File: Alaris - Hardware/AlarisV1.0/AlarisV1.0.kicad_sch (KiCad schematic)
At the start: 55 parts, among them J1 MSD-1-A, J2 MTSW-101, J3 636101111001, Q1 BSS138, Q2 BSS138, U1 STM32F401RCTx, U2 BNO055, U3 BMP390L, U4 MS5611-01BA, U5 ICM-20948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

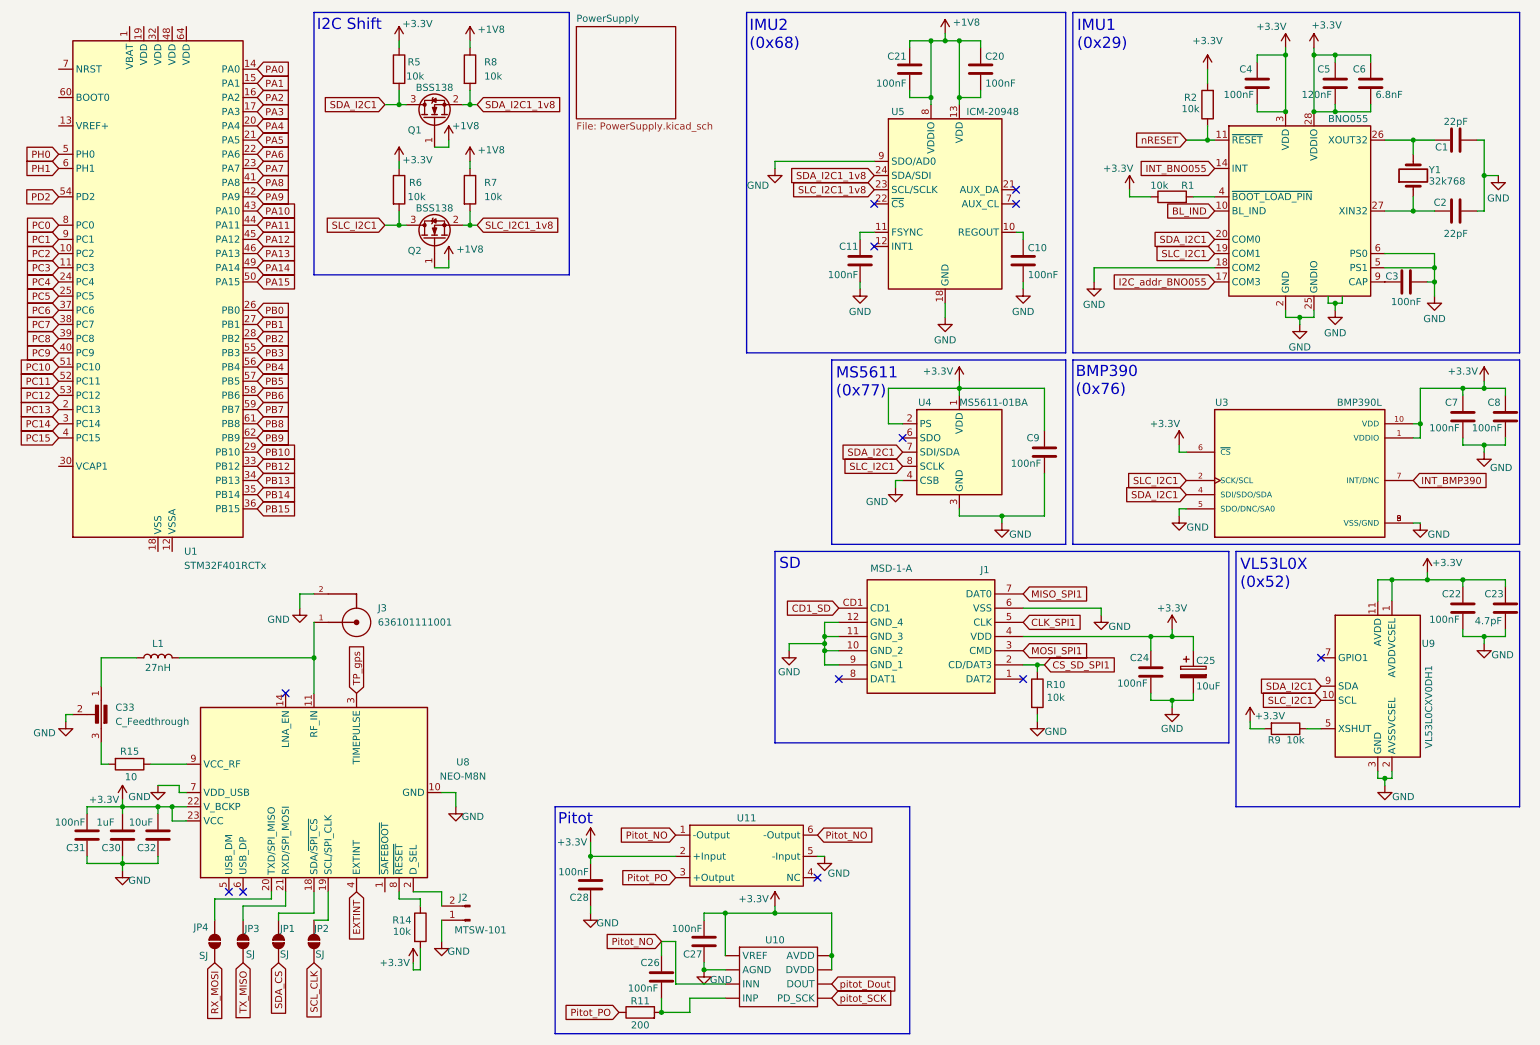
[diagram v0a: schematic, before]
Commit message: Desenvolvimento do Hardware
Desenvolvido os modulos de DAPN, GNCN, LDIN

Ainda é necessario implementação de alguns sensores, e melhor o modulo de gerenciamento de energia da placa
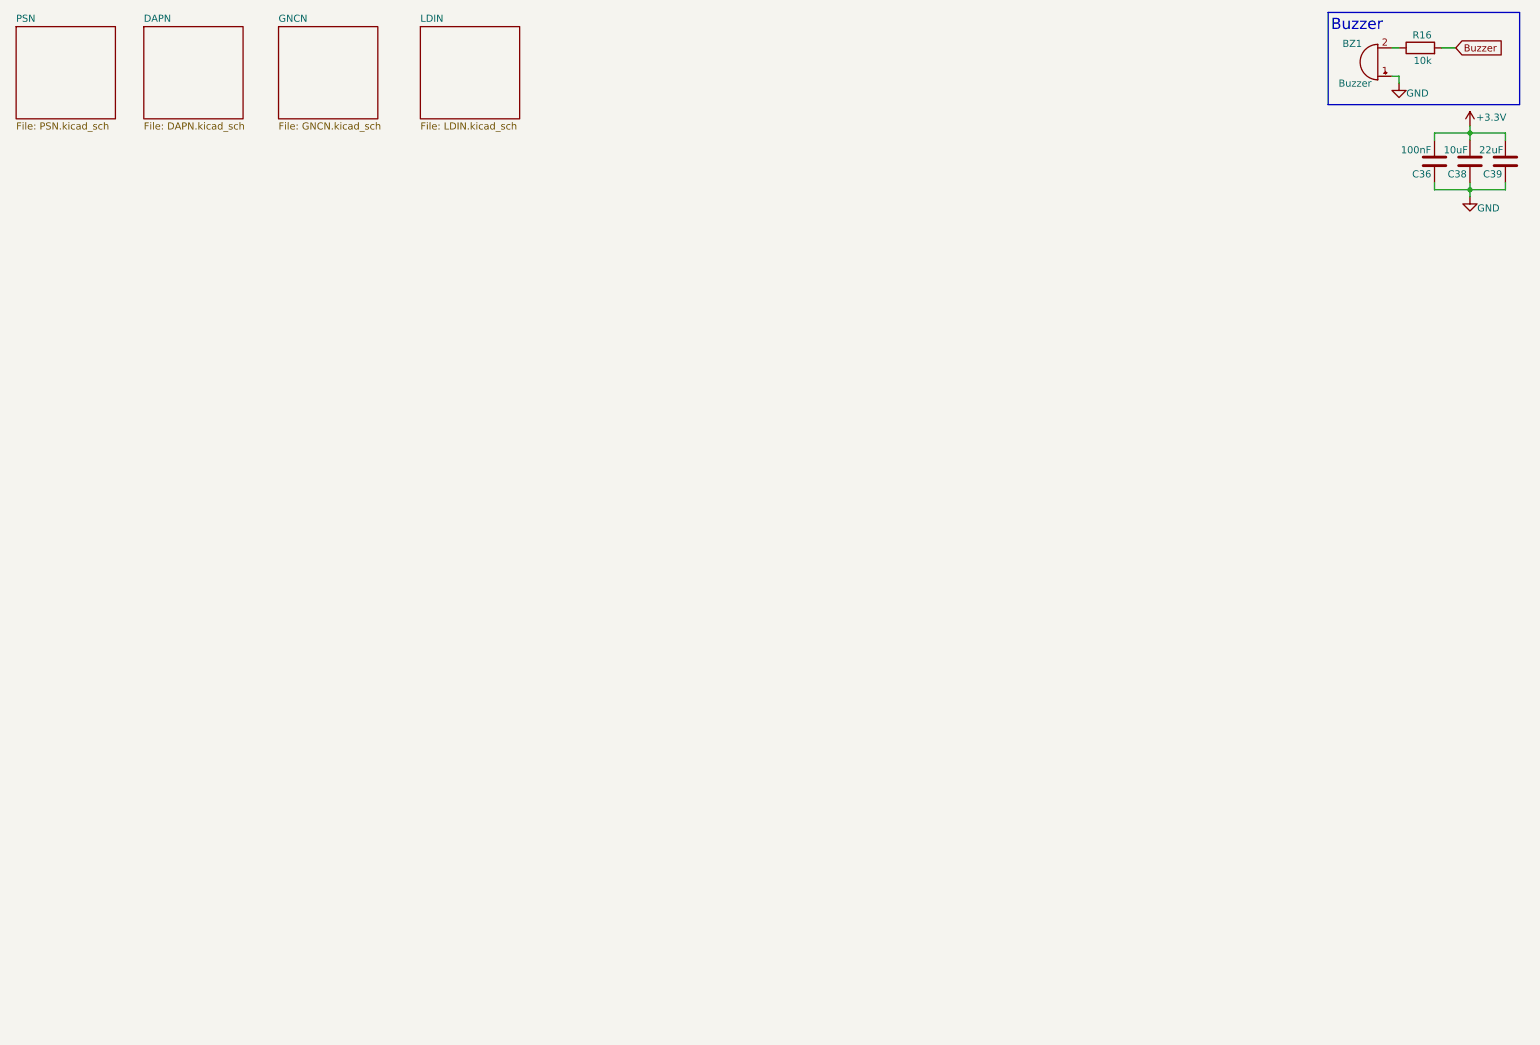
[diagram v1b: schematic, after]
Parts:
- removed C1, C2: 22pF, symbol Device:C
- removed C10, C11, C20, C21, C22, C24, C26, C27, C28, C3, C31, C4, C7, C8, C9: 100nF, symbol Device:C
- removed C23: 4.7pF, symbol Device:C
- removed C25: 10uF, symbol Device:C_Polarized
- removed C30: 1uF, symbol Device:C
- removed C32: 10uF, symbol Device:C
- removed C33: C_Feedthrough, symbol Device:C_Feedthrough
- removed C5: 120nF, symbol Device:C
- removed C6: 6.8nF, symbol Device:C
- removed J1: MSD-1-A, MSD1A, symbol MSD-1-A:MSD-1-A
- removed J2: MTSW-101, symbol Connector:Conn_01x02_Pin
- removed J3: 636101111001, 636101111001:636101111001, symbol 636101111001:636101111001
- removed JP1, JP2, JP3, JP4: SJ, symbol Jumper:SolderJumper_2_Open
- removed L1: 27nH, symbol Device:L
- removed Q1, Q2: BSS138, Package_TO_SOT_SMD:SOT-23, symbol Transistor_FET:BSS138
- removed R1, R10, R14, R2, R5, R6, R7, R8, R9: 10k, symbol Device:R
- removed R11: 200, symbol Device:R
- removed R15: 10, symbol Device:R
- removed U1: STM32F401RCTx, Package_QFP:LQFP-64_10x10mm_P0.5mm, symbol MCU_ST_STM32F4:STM32F401RCTx
- removed U10: ~, symbol SensoresMeus:HX710
- removed U11: ~, symbol SensoresMeus:MPS20N0040D-S
- removed U2: BNO055, Package_LGA:LGA-28_5.2x3.8mm_P0.5mm, symbol Sensor_Motion:BNO055
- removed U3: BMP390L, BMP390L:XDCR_BMP390L, symbol BMP390L:BMP390L
- removed U4: MS5611-01BA, Package_LGA:LGA-8_3x5mm_P1.25mm, symbol Sensor_Pressure:MS5611-01BA
- removed U5: ICM-20948, Sensor_Motion:InvenSense_QFN-24_3x3mm_P0.4mm, symbol Sensor_Motion:ICM-20948
- removed U8: NEO-M8N, RF_GPS:ublox_NEO, symbol RF_GPS:NEO-M8N
- removed U9: VL53L0CXV0DH1, Sensor_Distance:ST_VL53L1x, symbol Sensor_Distance:VL53L0CXV0DH1
- removed Y1: 32k768, symbol Device:Crystal
- added BZ1: Buzzer, symbol Device:Buzzer
- added C36: 100nF, Capacitor_SMD:C_0603_1608Metric_Pad1.08x0.95mm_HandSolder, symbol Device:C
- added C38: 10uF, Capacitor_SMD:C_0603_1608Metric_Pad1.08x0.95mm_HandSolder, symbol Device:C
- added C39: 22uF, Capacitor_SMD:C_0603_1608Metric_Pad1.08x0.95mm_HandSolder, symbol Device:C
- added R16: 10k, Resistor_SMD:R_0603_1608Metric_Pad0.98x0.95mm_HandSolder, symbol Device:R
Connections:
- net +3.3V: now also C36.2, C38.2, C39.2
- net GND: now also BZ1.1 (+), C36.1, C38.1, C39.1
- new net: BZ1.2 (-), R16.1
- new net Buzzer: R16.2
- no-connect marks 12 -> 0
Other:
- removed sheet PowerSupply
- added sheet DAPN (DAPN.kicad_sch)
- added sheet GNCN (GNCN.kicad_sch)
- added sheet LDIN (LDIN.kicad_sch)
- added sheet PSN (PSN.kicad_sch)
- note added: "Buzzer"
- note removed: "BMP390 (0x76)"
- note removed: "I2C Shift"
- note removed: "IMU1 (0x29)"
- note removed: "IMU2 (0x68)"
- note removed: "MS5611 (0x77)"
- note removed: "Pitot"
- note removed: "SD"
- note removed: "VL53L0X (0x52)"

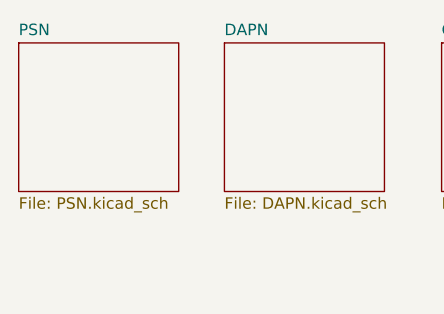
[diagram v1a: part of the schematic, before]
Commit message: Hardware and Software
Hardware: adição da proteção contra polaridade reversa
Software: Adição dos arquivos iniciais de projeto do LDIN
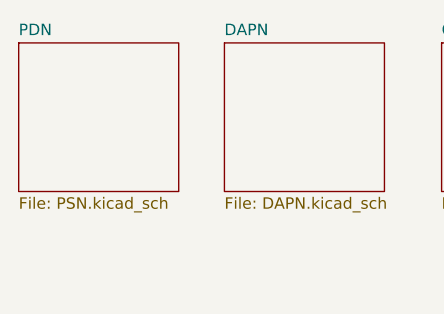
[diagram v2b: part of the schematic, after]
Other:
- sheet PSN renamed PDN
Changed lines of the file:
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@@
 			(color 0 0 0 0.0000)
 		)
-		(property "Sheetname" "PSN"
+		(property "Sheetname" "PDN"
 			(at 15.24 14.5284 0)
 			(effects

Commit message: Desenvolvimento da PCB
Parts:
- removed BZ1: Buzzer, symbol Device:Buzzer
- removed C36: 100nF, Capacitor_SMD:C_0603_1608Metric_Pad1.08x0.95mm_HandSolder, symbol Device:C
- removed C38: 10uF, Capacitor_SMD:C_0603_1608Metric_Pad1.08x0.95mm_HandSolder, symbol Device:C
- removed C39: 22uF, Capacitor_SMD:C_0603_1608Metric_Pad1.08x0.95mm_HandSolder, symbol Device:C
- added LS1: CMT-0525-75-SMT-TR, Footprint:Buzzer5mm, symbol Buzzer5mm:CMT-0525-75-SMT-TR
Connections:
- net GND: now also LS1.N
- net at R16.1: now also LS1.P
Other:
- note added: "SPI DAPN-GNC"
- note added: "UART DAPN-LDI"
- moved on the sheet: R16
